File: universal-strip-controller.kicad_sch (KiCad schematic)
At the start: 50 parts, among them J1 Conn_01x03_Pin, J2 Conn_01x02_Pin, SW1 434133025816, SW2 434133025816, U1 RP2350B, U2 RPI RM2, U3 W25Q128JVSIQ, U9 DS3231SN, X1 12MHz

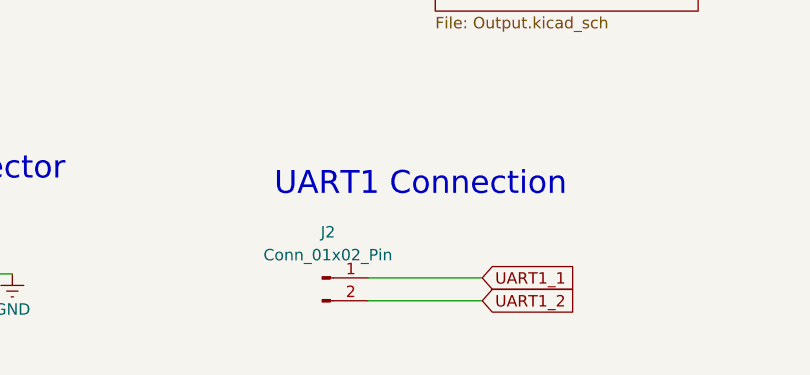
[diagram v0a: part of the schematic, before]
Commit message: Label J2 UART1 header pins as TX/RX
Adds text annotations next to J2 (the UART1 debug header) so pin 1
(GPIO36) and pin 2 (GPIO37) are marked TX/RX per the RP2350 UART1
function mapping, without changing the underlying net names.

Co-Authored-By: Claude Sonnet 5 <noreply@anthropic.com>
Claude-Session: https://claude.ai/code/session_01JtXLVspEAaAehFAxappY7R
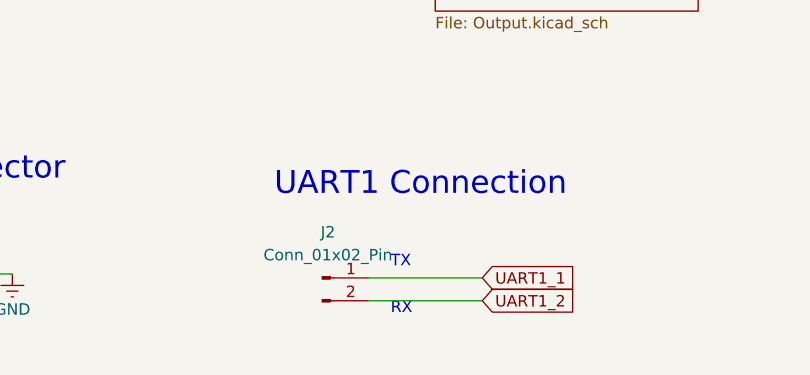
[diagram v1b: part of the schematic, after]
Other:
- note added: "RX"
- note added: "TX"
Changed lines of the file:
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@@
+		)
+	)
+	(text "TX"
+		(exclude_from_sim no)
+		(at 230.0 267.4 0)
+		(effects
+			(font
+				(size 1.27 1.27)
+			)
+			(justify left bottom)
+		)
+	)
+	(text "RX"
+		(exclude_from_sim no)
+		(at 230.0 272.6 0)
+		(effects
+			(font
+				(size 1.27 1.27)
+			)
+			(justify left bottom)
 		)
 	)
